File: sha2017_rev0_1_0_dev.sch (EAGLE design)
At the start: 117 parts, among them IC1 AP7215, IC2 CPT112, IC3 CP210X_USB_UART, IC4 ESP32WROOM32, IC5 MCP73833, IC6 FXL6408, Q1 MMBT2222A, Q2 MMBT2222A, Q3 SI1304 BDL, Q4 MOSFET-PCHANNEL, Q5 MMBT2222A, Q6 MOSFET-PCHANNEL, Q7 MMBT2222A, Q8 MMBT2222A, T1 SI2301DS, X1_ JST-PH3, X701 2908-05WB-MG

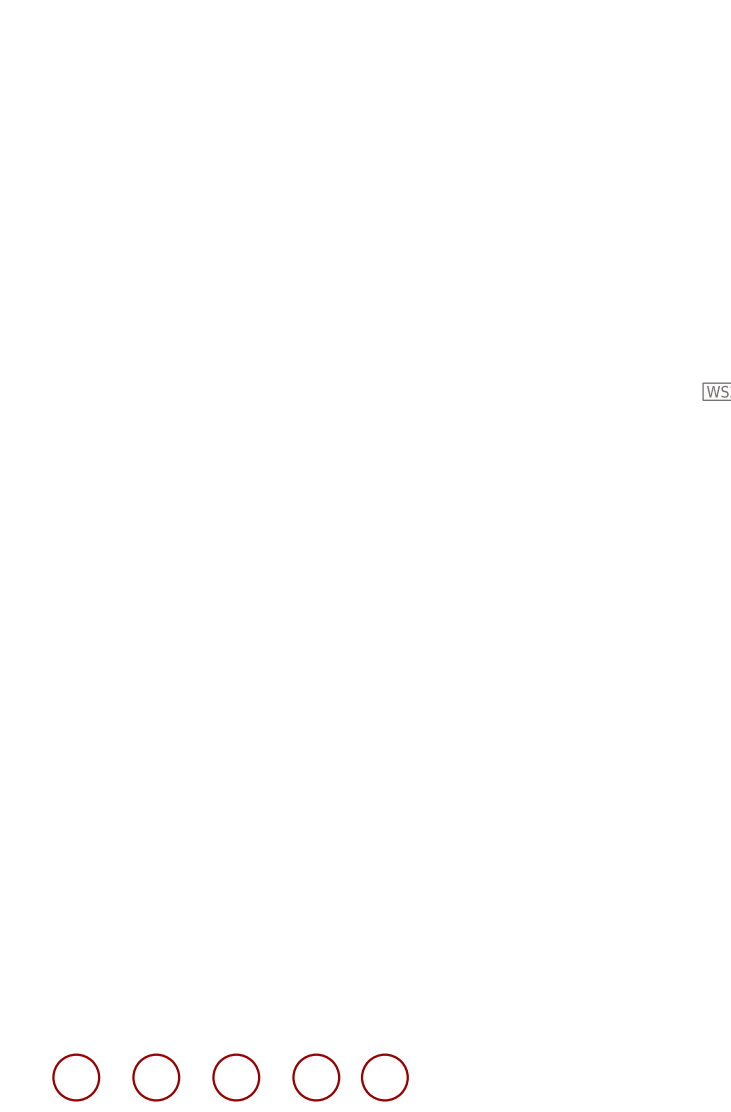
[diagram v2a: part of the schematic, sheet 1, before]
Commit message: add spezial vias to touch arrea to trick DRC
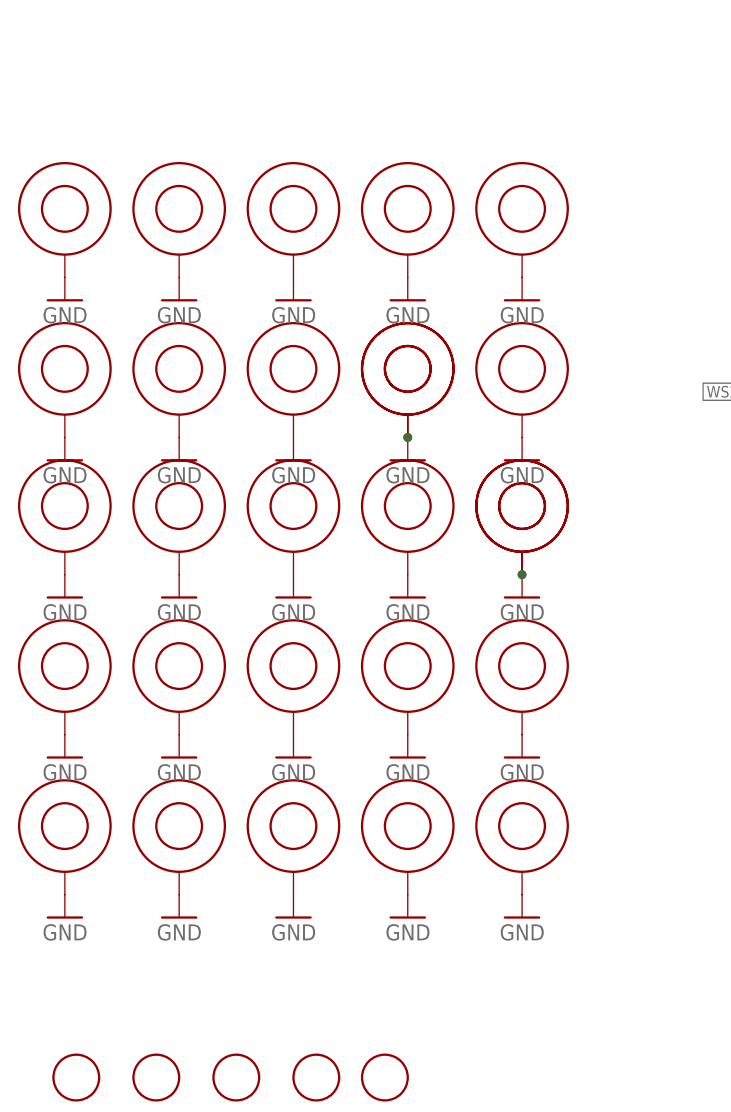
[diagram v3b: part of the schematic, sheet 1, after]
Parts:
- added U$10, U$11, U$12, U$13, U$14, U$15, U$16, U$17, U$18, U$19, U$2, U$20, U$21, U$22, U$23, U$24, U$25, U$26, U$27, U$28, U$29, U$3, U$30, U$31, U$4, U$5, U$6: VIA, badge:VIA
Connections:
- net GND: now also U$10.P$1, U$11.P$1, U$12.P$1, U$13.P$1, U$14.P$1, U$15.P$1, U$16.P$1, U$17.P$1, U$18.P$1, U$19.P$1, U$2.P$1, U$20.P$1, U$21.P$1, U$22.P$1, U$23.P$1, U$24.P$1, U$25.P$1, U$26.P$1, U$27.P$1, U$28.P$1, U$29.P$1, U$3.P$1, U$30.P$1, U$31.P$1, U$4.P$1, U$5.P$1, U$6.P$1
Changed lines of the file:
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@@
 <part name="GND60" library="supply1" deviceset="GND" device=""/>
 <part name="J3" library="EAGLE-BOARD-TO-BOARD_CONNECTORS-rev16c" deviceset="610X12243021" device=""/>
+<part name="U$2" library="badge" deviceset="VIA" device=""/>
+<part name="U$3" library="badge" deviceset="VIA" device=""/>
+<part name="U$4" library="badge" deviceset="VIA" device=""/>
+<part name="U$5" library="badge" deviceset="VIA" device=""/>
+<part name="U$6" library="badge" deviceset="VIA" device=""/>
+<part name="U$10" library="badge" deviceset="VIA" device=""/>
+<part name="U$11" library="badge" deviceset="VIA" device=""/>
+<part name="U$12" library="badge" deviceset="VIA" device=""/>
+<part name="U$13" library="badge" deviceset="VIA" device=""/>
+<part name="U$14" library="badge" deviceset="VIA" device=""/>
+<part name="U$15" library="badge" deviceset="VIA" device=""/>
+<part name="U$16" library="badge" deviceset="VIA" device=""/>
+<part name="U$17" library="badge" deviceset="VIA" device=""/>
+<part name="U$18" library="badge" deviceset="VIA" device=""/>
+<part name="U$19" library="badge" deviceset="VIA" device=""/>
+<part name="U$20" library="badge" deviceset="VIA" device=""/>
+<part name="GND62" library="supply1" deviceset="GND" device=""/>
+<part name="GND63" library="supply1" deviceset="GND" device=""/>
+<part name="GND64" library="supply1" deviceset="GND" device=""/>
+<part name="GND65" library="supply1" deviceset="GND" device=""/>
+<part name="GND66" library="supply1" deviceset="GND" device=""/>
+<part name="GND67" library="supply1" deviceset="GND" device=""/>
+<part name="GND68" library="supply1" deviceset="GND" device=""/>
+<part name="GND69" library="supply1" deviceset="GND" device=""/>
+<part name="GND70" library="supply1" deviceset="GND" device=""/>
+<part name="GND71" library="supply1" deviceset="GND" device=""/>
+<part name="GND72" library="supply1" deviceset="GND" device=""/>
+<part name="GND73" library="supply1" deviceset="GND" device=""/>
+<part name="GND74" library="supply1" deviceset="GND" device=""/>
+<part name="GND75" library="supply1" deviceset="GND" device=""/>
+<part name="GND76" library="supply1" deviceset="GND" device=""/>
+<part name="U$21" library="badge" deviceset="VIA" device=""/>
+<part name="U$22" library="badge" deviceset="VIA" device=""/>
+<part name="U$23" library="badge" deviceset="VIA" device=""/>
+<part name="U$24" library="badge" deviceset="VIA" device=""/>
+<part name="U$25" library="badge" deviceset="VIA" device=""/>
+<part name="U$26" library="badge" deviceset="VIA" device=""/>
+<part name="GND77" library="supply1" deviceset="GND" device=""/>
+<part name="GND78" library="supply1" deviceset="GND" device=""/>
+<part name="GND79" library="supply1" deviceset="GND" device=""/>
+<part name="GND80" library="supply1" deviceset="GND" device=""/>
+<part name="GND81" library="supply1" deviceset="GND" device=""/>
+<part name="U$27" library="badge" deviceset="VIA" device=""/>
+<part name="U$28" library="badge" deviceset="VIA" device=""/>
+<part name="U$29" library="badge" deviceset="VIA" device=""/>
+<part name="U$30" library="badge" deviceset="VIA" device=""/>
+<part name="U$31" library="badge" deviceset="VIA" device=""/>
+<part name="GND82" library="supply1" deviceset="GND" device=""/>
+<part name="GND83" library="supply1" deviceset="GND" device=""/>
+<part name="GND84" library="supply1" deviceset="GND" device=""/>
+<part name="GND85" library="supply1" deviceset="GND" device=""/>
+<part name="GND86" library="supply1" deviceset="GND" device=""/>
 </parts>
 <sheets>
@@
 <instance part="S2" gate="G$1" x="177.8" y="147.32"/>
 <instance part="GND60" gate="1" x="170.18" y="142.24"/>
+<instance part="U$2" gate="G$1" x="66.04" y="55.88"/>
+<instance part="U$3" gate="G$1" x="15.24" y="38.1"/>
+<instance part="U$4" gate="G$1" x="27.94" y="38.1"/>
+<instance part="U$5" gate="G$1" x="40.64" y="38.1"/>
+<instance part="U$6" gate="G$1" x="53.34" y="38.1"/>
+<instance part="U$10" gate="G$1" x="66.04" y="38.1"/>
+<instance part="U$11" gate="G$1" x="15.24" y="55.88"/>
+<instance part="U$12" gate="G$1" x="27.94" y="55.88"/>
+<instance part="U$13" gate="G$1" x="40.64" y="55.88"/>
+<instance part="U$14" gate="G$1" x="53.34" y="55.88"/>
+<instance part="U$15" gate="G$1" x="15.24" y="73.66"/>
+<instance part="U$16" gate="G$1" x="27.94" y="73.66"/>
+<instance part="U$17" gate="G$1" x="40.64" y="73.66"/>
+<instance part="U$18" gate="G$1" x="53.34" y="73.66"/>
+<instance part="U$19" gate="G$1" x="66.04" y="73.66"/>
+<instance part="U$20" gate="G$1" x="66.04" y="73.66"/>
+<instance part="GND62" gate="1" x="15.24" y="63.5" rot="MR0"/>
+<instance part="GND63" gate="1" x="27.94" y="63.5" rot="MR0"/>
+<instance part="GND64" gate="1" x="40.64" y="63.5" rot="MR0"/>
+<instance part="GND65" gate="1" x="53.34" y="63.5" rot="MR0"/>
+<instance part="GND66" gate="1" x="66.04" y="63.5" rot="MR0"/>
+<instance part="GND67" gate="1" x="15.24" y="45.72" rot="MR0"/>
+<instance part="GND68" gate="1" x="27.94" y="45.72" rot="MR0"/>
+<instance part="GND69" gate="1" x="40.64" y="45.72" rot="MR0"/>
+<instance part="GND70" gate="1" x="53.34" y="45.72" rot="MR0"/>
+<instance part="GND71" gate="1" x="66.04" y="45.72" rot="MR0"/>
+<instance part="GND72" gate="1" x="66.04" y="27.94" rot="MR0"/>
+<instance part="GND73" gate="1" x="53.34" y="27.94" rot="MR0"/>
+<instance part="GND74" gate="1" x="40.64" y="27.94" rot="MR0"/>
+<instance part="GND75" gate="1" x="27.94" y="27.94" rot="MR0"/>
+<instance part="GND76" gate="1" x="15.24" y="27.94" rot="MR0"/>
+<instance part="U$21" gate="G$1" x="15.24" y="88.9"/>
+<instance part="U$22" gate="G$1" x="27.94" y="88.9"/>
+<instance part="U$23" gate="G$1" x="40.64" y="88.9"/>
+<instance part="U$24" gate="G$1" x="53.34" y="88.9"/>
+<instance part="U$25" gate="G$1" x="53.34" y="88.9"/>
+<instance part="U$26" gate="G$1" x="66.04" y="88.9"/>
+<instance part="GND77" gate="1" x="15.24" y="78.74" rot="MR0"/>
+<instance part="GND78" gate="1" x="27.94" y="78.74" rot="MR0"/>
+<instance part="GND79" gate="1" x="40.64" y="78.74" rot="MR0"/>
+<instance part="GND80" gate="1" x="53.34" y="78.74" rot="MR0"/>
+<instance part="GND81" gate="1" x="66.04" y="78.74" rot="MR0"/>
+<instance part="U$27" gate="G$1" x="15.24" y="106.68"/>
+<instance part="U$28" gate="G$1" x="27.94" y="106.68"/>
+<instance part="U$29" gate="G$1" x="40.64" y="106.68"/>
+<instance part="U$30" gate="G$1" x="53.34" y="106.68"/>
+<instance part="U$31" gate="G$1" x="66.04" y="106.68"/>
+<instance part="GND82" gate="1" x="15.24" y="96.52" rot="MR0"/>
+<instance part="GND83" gate="1" x="27.94" y="96.52" rot="MR0"/>
+<instance part="GND84" gate="1" x="40.64" y="96.52" rot="MR0"/>
+<instance part="GND85" gate="1" x="53.34" y="96.52" rot="MR0"/>
+<instance part="GND86" gate="1" x="66.04" y="96.52" rot="MR0"/>
 </instances>
 <busses>
@@
 <pinref part="GND60" gate="1" pin="GND"/>
 </segment>
+<segment>
+<pinref part="U$15" gate="G$1" pin="P$1"/>
+<pinref part="GND62" gate="1" pin="GND"/>
+</segment>
+<segment>
+<pinref part="U$16" gate="G$1" pin="P$1"/>
+<pinref part="GND63" gate="1" pin="GND"/>
+</segment>
+<segment>
+<pinref part="U$17" gate="G$1" pin="P$1"/>
+<pinref part="GND64" gate="1" pin="GND"/>
+</segment>
+<segment>
+<pinref part="U$18" gate="G$1" pin="P$1"/>
+<pinref part="GND65" gate="1" pin="GND"/>
+</segment>
+<segment>
+<pinref part="U$19" gate="G$1" pin="P$1"/>
+<pinref part="U$20" gate="G$1" pin="P$1"/>
+<pinref part="GND66" gate="1" pin="GND"/>
+<junction x="66.04" y="66.04"/>
+<pinref part="GND66" gate="1" pin="GND"/>
+</segment>
+<segment>
+<pinref part="U$11" gate="G$1" pin="P$1"/>
+<pinref part="GND67" gate="1" pin="GND"/>
+</segment>
+<segment>
+<pinref part="U$12" gate="G$1" pin="P$1"/>
+<pinref part="GND68" gate="1" pin="GND"/>
+</segment>
+<segment>
+<pinref part="U$13" gate="G$1" pin="P$1"/>
+<pinref part="GND69" gate="1" pin="GND"/>
+</segment>
+<segment>
+<pinref part="U$14" gate="G$1" pin="P$1"/>
+<pinref part="GND70" gate="1" pin="GND"/>
+</segment>
+<segment>
+<pinref part="U$2" gate="G$1" pin="P$1"/>
+<pinref part="GND71" gate="1" pin="GND"/>
+</segment>
+<segment>
+<pinref part="U$10" gate="G$1" pin="P$1"/>
+<pinref part="GND72" gate="1" pin="GND"/>
+</segment>
+<segment>
+<pinref part="U$6" gate="G$1" pin="P$1"/>
+<pinref part="GND73" gate="1" pin="GND"/>
+</segment>
+<segment>
+<pinref part="U$5" gate="G$1" pin="P$1"/>
+<pinref part="GND74" gate="1" pin="GND"/>
+</segment>
+<segment>
+<pinref part="U$4" gate="G$1" pin="P$1"/>
+<pinref part="GND75" gate="1" pin="GND"/>
+</segment>
+<segment>
+<pinref part="U$3" gate="G$1" pin="P$1"/>
+<pinref part="GND76" gate="1" pin="GND"/>
+</segment>
+<segment>
+<pinref part="U$21" gate="G$1" pin="P$1"/>
+<pinref part="GND77" gate="1" pin="GND"/>
+</segment>
+<segment>
+<pinref part="U$22" gate="G$1" pin="P$1"/>
+<pinref part="GND78" gate="1" pin="GND"/>
+</segment>
+<segment>
+<pinref part="U$23" gate="G$1" pin="P$1"/>
+<pinref part="GND79" gate="1" pin="GND"/>
+</segment>
+<segment>
+<pinref part="U$24" gate="G$1" pin="P$1"/>
+<pinref part="U$25" gate="G$1" pin="P$1"/>
+<pinref part="GND80" gate="1" pin="GND"/>
+<junction x="53.34" y="81.28"/>
+<pinref part="GND80" gate="1" pin="GND"/>
+</segment>
+<segment>
+<pinref part="U$26" gate="G$1" pin="P$1"/>
+<pinref part="GND81" gate="1" pin="GND"/>
+</segment>
+<segment>
+<pinref part="U$27" gate="G$1" pin="P$1"/>
+<pinref part="GND82" gate="1" pin="GND"/>
+</segment>
+<segment>
+<pinref part="U$28" gate="G$1" pin="P$1"/>
+<pinref part="GND83" gate="1" pin="GND"/>
+</segment>
+<segment>
+<pinref part="U$29" gate="G$1" pin="P$1"/>
+<pinref part="GND84" gate="1" pin="GND"/>
+</segment>
+<segment>
+<pinref part="U$30" gate="G$1" pin="P$1"/>
+<pinref part="GND85" gate="1" pin="GND"/>
+</segment>
+<segment>
+<pinref part="U$31" gate="G$1" pin="P$1"/>
+<pinref part="GND86" gate="1" pin="GND"/>
+</segment>
 </net>

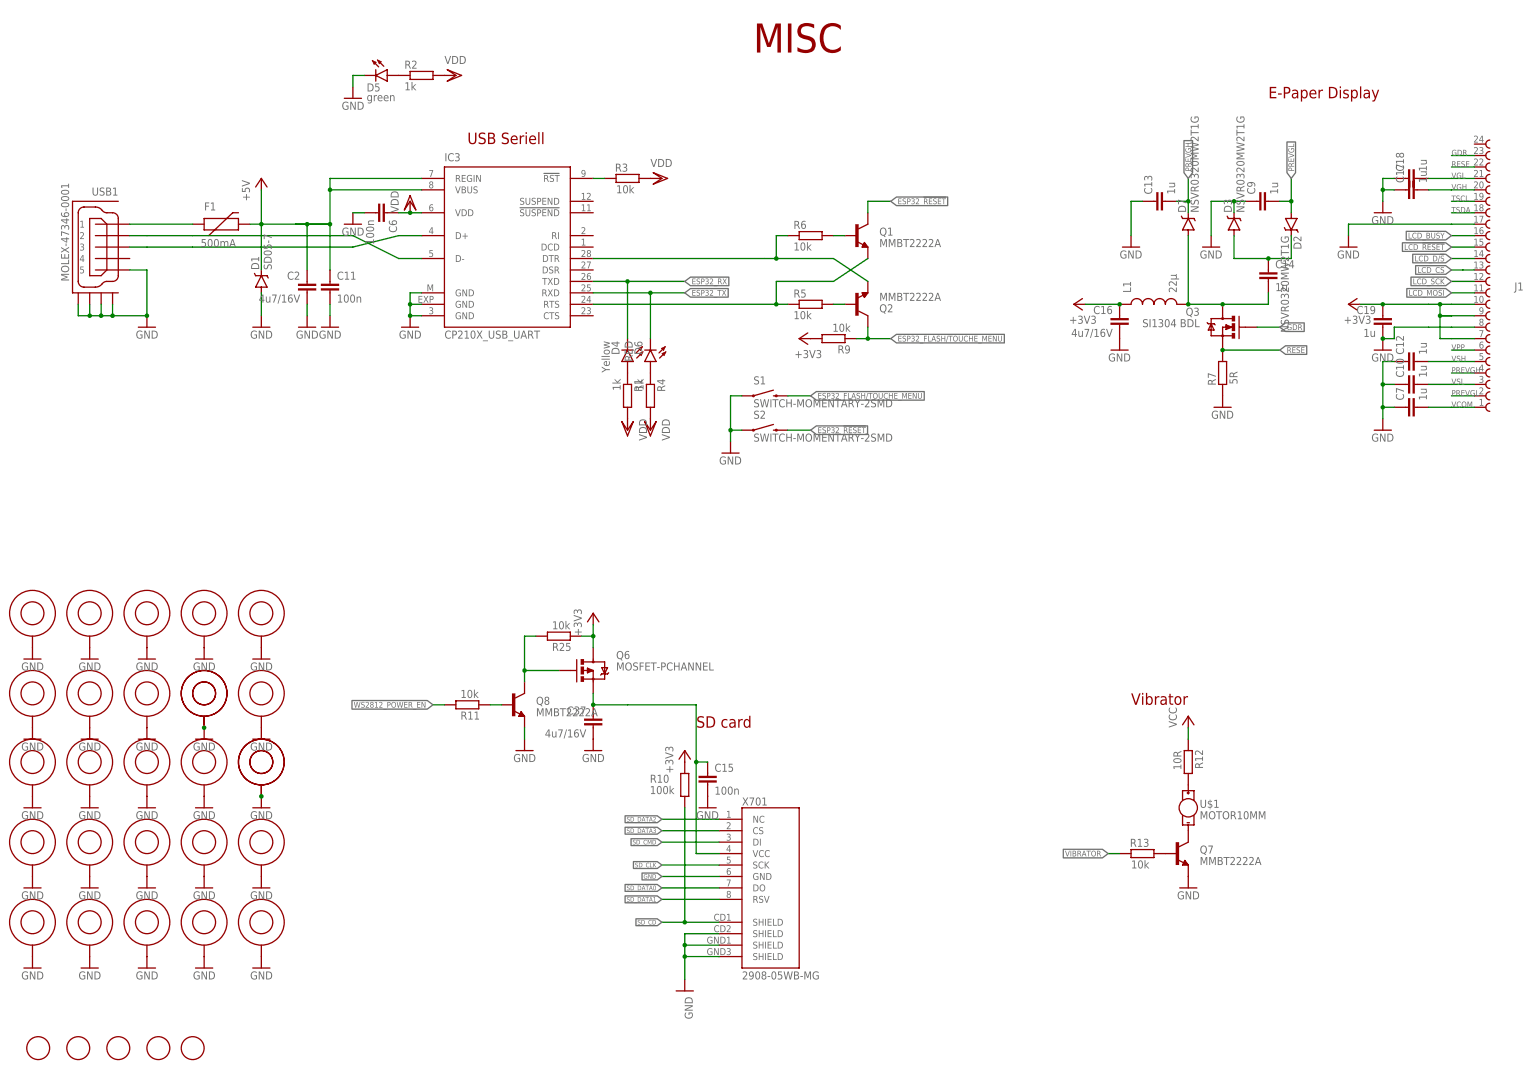
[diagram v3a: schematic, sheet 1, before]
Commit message: added most of the test points
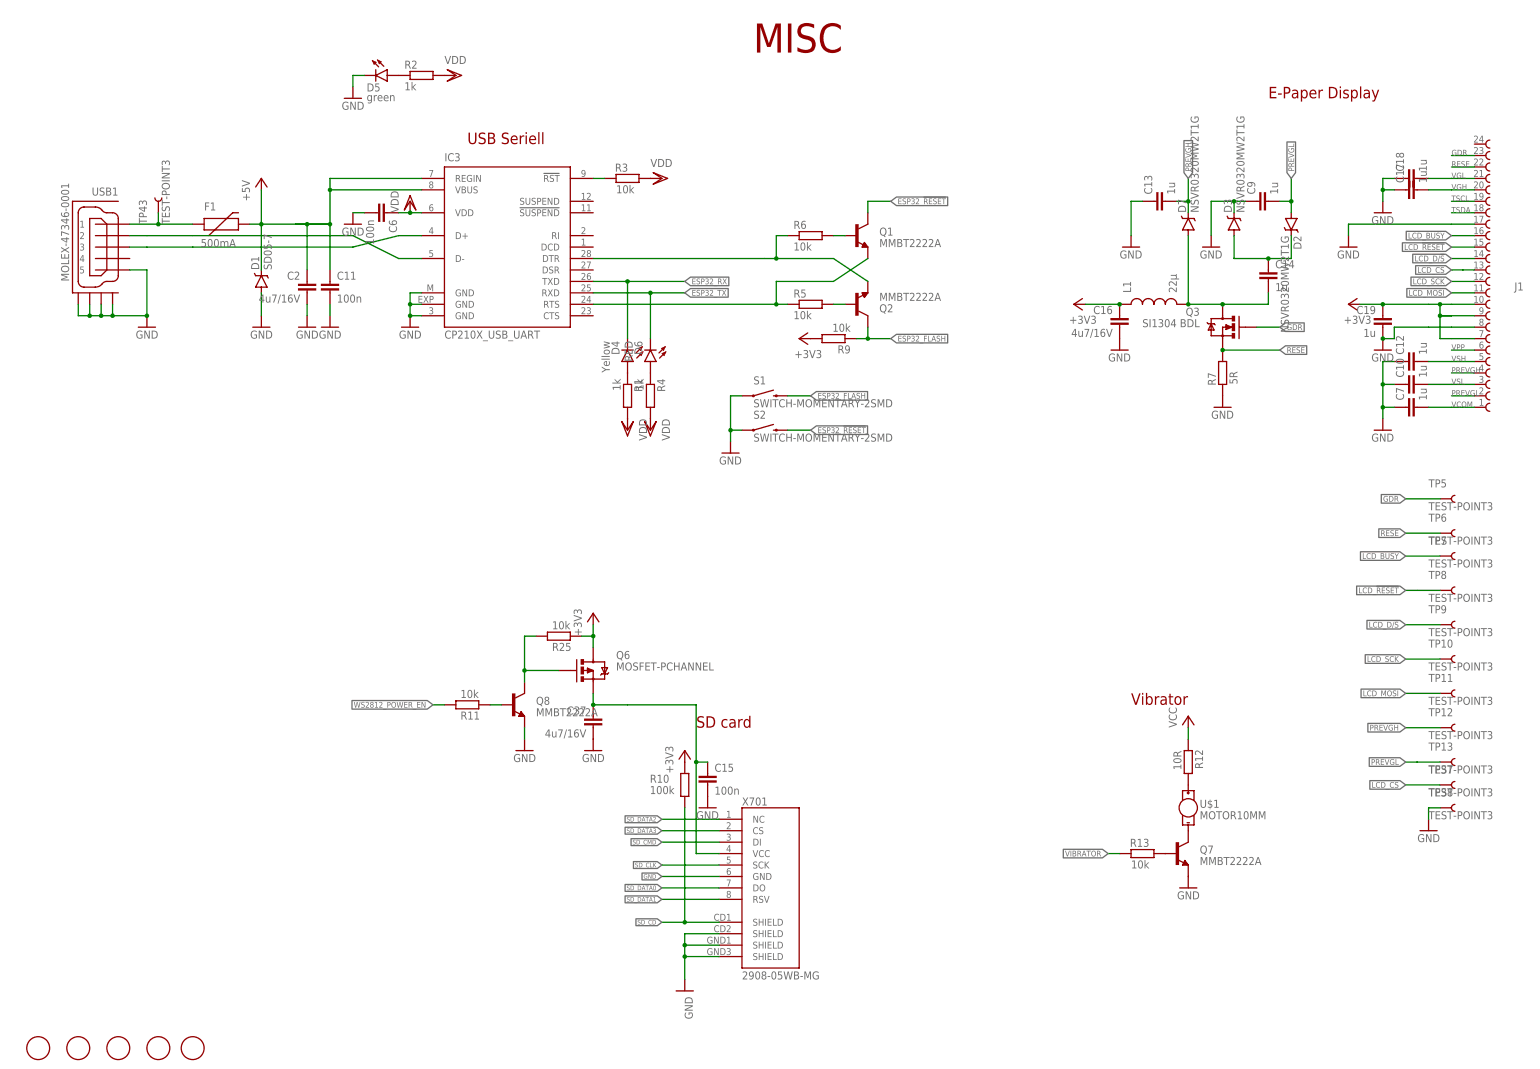
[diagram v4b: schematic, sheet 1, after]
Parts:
- added TP10, TP11, TP12, TP13, TP14, TP15, TP16, TP17, TP18, TP19, TP20, TP22, TP23, TP24, TP25, TP26, TP27, TP28, TP29, TP3, TP30, TP31, TP32, TP33, TP34, TP35, TP36, TP37, TP38, TP39, TP4, TP40, TP41, TP42, TP43, TP5, TP6, TP7, TP8, TP9: TEST-POINT3, SparkFun-Passives:TEST-POINT3
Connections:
- removed net ESP32_FLASH/TOUCHE_MENU: IC4.IO0, Q2.C, R9.1, S1.2
- new net ESP32_FLASH: IC4.IO0, Q2.C, R9.1, S1.2, TP23.1
- net +3V3: now also TP28.1
- net +5V: now also TP30.1
- net 3V3_SWITCHED: now also TP26.1
- net ESP32_!RESET: now also TP24.1
- net ESP32_RX: now also TP33.1
- net ESP32_TX: now also TP34.1
- net GDR: now also TP5.1
- net GND: now also TP32.1, TP38.1, TP39.1, TP40.1, TP41.1, TP42.1
- net I2C_SCL: now also TP20.1
- net I2C_SDA: now also TP22.1
- net LCD_!RESET: now also TP8.1
- net LCD_BUSY: now also TP7.1
- net LCD_CS: now also TP37.1
- net LCD_D/!S: now also TP9.1
- net LCD_MOSI: now also TP11.1
- net LCD_SCK: now also TP10.1
- net N$12: now also TP14.1
- net N$3: now also TP19.1
- net N$32: now also TP43.1
- net N$4: now also TP18.1
- net N$6: now also TP17.1
- net N$61: now also TP3.1
- net N$62: now also TP4.1
- net N$7: now also TP16.1
- net N$9: now also TP15.1
- net PREVGH: now also TP12.1
- net PREVGL: now also TP13.1
- net RESE: now also TP6.1
- net USB_DN_CON: now also TP35.1
- net USB_DP_CON: now also TP36.1
- net VBAT: now also TP27.1
- net VCC: now also TP29.1
- net WS2812_DATA: now also TP31.1
- net WS2812_POWER: now also TP25.1
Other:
- moved on the sheet: TP1, TP2
